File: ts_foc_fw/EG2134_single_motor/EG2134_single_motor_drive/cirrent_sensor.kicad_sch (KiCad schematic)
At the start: 6 parts, among them U4 TP181A1-CR, U5 TP181A1-CR

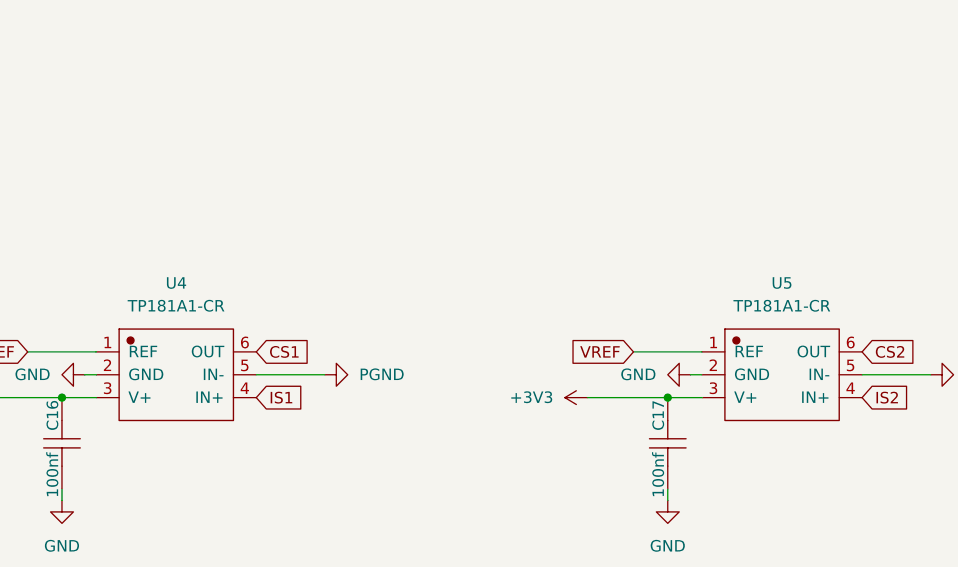
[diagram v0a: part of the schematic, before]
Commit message: PCB布局完成，等待布线
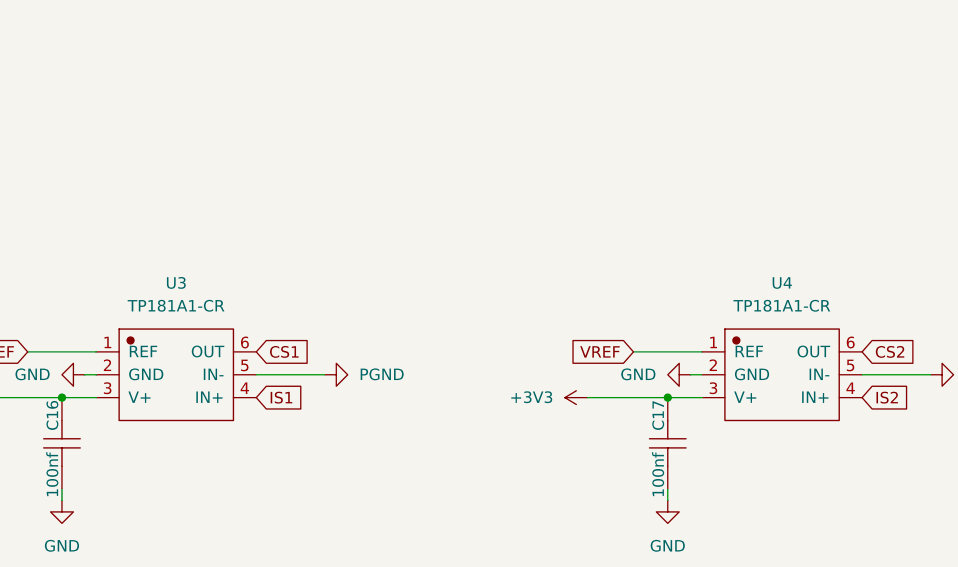
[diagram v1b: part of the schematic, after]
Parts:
- renumbered U4 to U3, U5 to U4
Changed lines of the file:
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@@
 		(dnp no)
 		(fields_autoplaced yes)
-		(property "Reference" "#PWR032"
+		(property "Reference" "#PWR025"
 			(at 114.3 67.31 0)
 			(effects
@@
 			(project ""
 				(path "/a69a3027-f6f2-4dc7-8446-d1a07c691b27/21110f3f-8b94-4208-8823-8df462e77b18"
-					(reference "#PWR032")
+					(reference "#PWR025")
 					(unit 1)
 				)
@@
 		(dnp no)
 		(fields_autoplaced yes)
-		(property "Reference" "U5"
+		(property "Reference" "U4"
 			(at 158.75 57.15 0)
 			(effects
@@
 			(project "EG2134_single_motor_drive"
 				(path "/a69a3027-f6f2-4dc7-8446-d1a07c691b27/21110f3f-8b94-4208-8823-8df462e77b18"
-					(reference "U5")
+					(reference "U4")
 					(unit 1)
 				)
@@
 		(dnp no)
 		(fields_autoplaced yes)
-		(property "Reference" "#PWR034"
+		(property "Reference" "#PWR027"
 			(at 146.05 87.63 0)
 			(effects
@@
 			(project "EG2134_single_motor_drive"
 				(path "/a69a3027-f6f2-4dc7-8446-d1a07c691b27/21110f3f-8b94-4208-8823-8df462e77b18"
-					(reference "#PWR034")
+					(reference "#PWR027")
 					(unit 1)
 				)
@@
 		(dnp no)
 		(fields_autoplaced yes)
-		(property "Reference" "#PWR037"
+		(property "Reference" "#PWR020"
 			(at 39.37 62.23 0)
 			(effects
@@
 			(project "EG2134_single_motor_drive"
 				(path "/a69a3027-f6f2-4dc7-8446-d1a07c691b27/21110f3f-8b94-4208-8823-8df462e77b18"
-					(reference "#PWR037")
+					(reference "#PWR020")
 					(unit 1)
 				)
@@
 		(dnp no)
 		(fields_autoplaced yes)
-		(property "Reference" "U4"
+		(property "Reference" "U3"
 			(at 91.44 57.15 0)
 			(effects
@@
 			(project ""
 				(path "/a69a3027-f6f2-4dc7-8446-d1a07c691b27/21110f3f-8b94-4208-8823-8df462e77b18"
-					(reference "U4")
+					(reference "U3")
 					(unit 1)
 				)
@@
 		(dnp no)
 		(fields_autoplaced yes)
-		(property "Reference" "#PWR033"
+		(property "Reference" "#PWR026"
 			(at 140.97 69.85 0)
 			(effects
@@
 			(project "EG2134_single_motor_drive"
 				(path "/a69a3027-f6f2-4dc7-8446-d1a07c691b27/21110f3f-8b94-4208-8823-8df462e77b18"
-					(reference "#PWR033")
+					(reference "#PWR026")
 					(unit 1)
 				)
@@
 		(dnp no)
 		(fields_autoplaced yes)
-		(property "Reference" "#PWR036"
+		(property "Reference" "#PWR029"
 			(at 181.61 67.31 0)
 			(effects
@@
 			(project "EG2134_single_motor_drive"
 				(path "/a69a3027-f6f2-4dc7-8446-d1a07c691b27/21110f3f-8b94-4208-8823-8df462e77b18"
-					(reference "#PWR036")
+					(reference "#PWR029")
 					(unit 1)
 				)
@@
 		(dnp no)
 		(fields_autoplaced yes)
-		(property "Reference" "#PWR031"
+		(property "Reference" "#PWR024"
 			(at 74.93 67.31 0)
 			(effects
@@
 			(project "EG2134_single_motor_drive"
 				(path "/a69a3027-f6f2-4dc7-8446-d1a07c691b27/21110f3f-8b94-4208-8823-8df462e77b18"
-					(reference "#PWR031")
+					(reference "#PWR024")
 					(unit 1)
 				)
@@
 		(dnp no)
 		(fields_autoplaced yes)
-		(property "Reference" "#PWR029"
+		(property "Reference" "#PWR023"
 			(at 78.74 87.63 0)
 			(effects
@@
 			(project ""
 				(path "/a69a3027-f6f2-4dc7-8446-d1a07c691b27/21110f3f-8b94-4208-8823-8df462e77b18"
-					(reference "#PWR029")
+					(reference "#PWR023")
 					(unit 1)
 				)
@@
 		(dnp no)
 		(fields_autoplaced yes)
-		(property "Reference" "#PWR030"
+		(property "Reference" "#PWR022"
 			(at 73.66 69.85 0)
 			(effects
@@
 			(project ""
 				(path "/a69a3027-f6f2-4dc7-8446-d1a07c691b27/21110f3f-8b94-4208-8823-8df462e77b18"
-					(reference "#PWR030")
+					(reference "#PWR022")
 					(unit 1)
 				)
@@
 		(dnp no)
 		(fields_autoplaced yes)
-		(property "Reference" "#PWR035"
+		(property "Reference" "#PWR028"
 			(at 142.24 67.31 0)
 			(effects
@@
 			(project "EG2134_single_motor_drive"
 				(path "/a69a3027-f6f2-4dc7-8446-d1a07c691b27/21110f3f-8b94-4208-8823-8df462e77b18"
-					(reference "#PWR035")
+					(reference "#PWR028")
 					(unit 1)
 				)
@@
 		(dnp no)
 		(fields_autoplaced yes)
-		(property "Reference" "#PWR038"
+		(property "Reference" "#PWR021"
 			(at 39.37 93.98 0)
 			(effects
@@
 			(project ""
 				(path "/a69a3027-f6f2-4dc7-8446-d1a07c691b27/21110f3f-8b94-4208-8823-8df462e77b18"
-					(reference "#PWR038")
-					(unit 1)
-				)
+					(reference "#PWR021")
+					(unit 1)
+				)
